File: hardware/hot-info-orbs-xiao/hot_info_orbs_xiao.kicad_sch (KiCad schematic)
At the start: 10 parts, among them SW1 SW_Push, SW2 SW_Push, SW3 SW_Push, U2 ESP32-S3-SuperMini

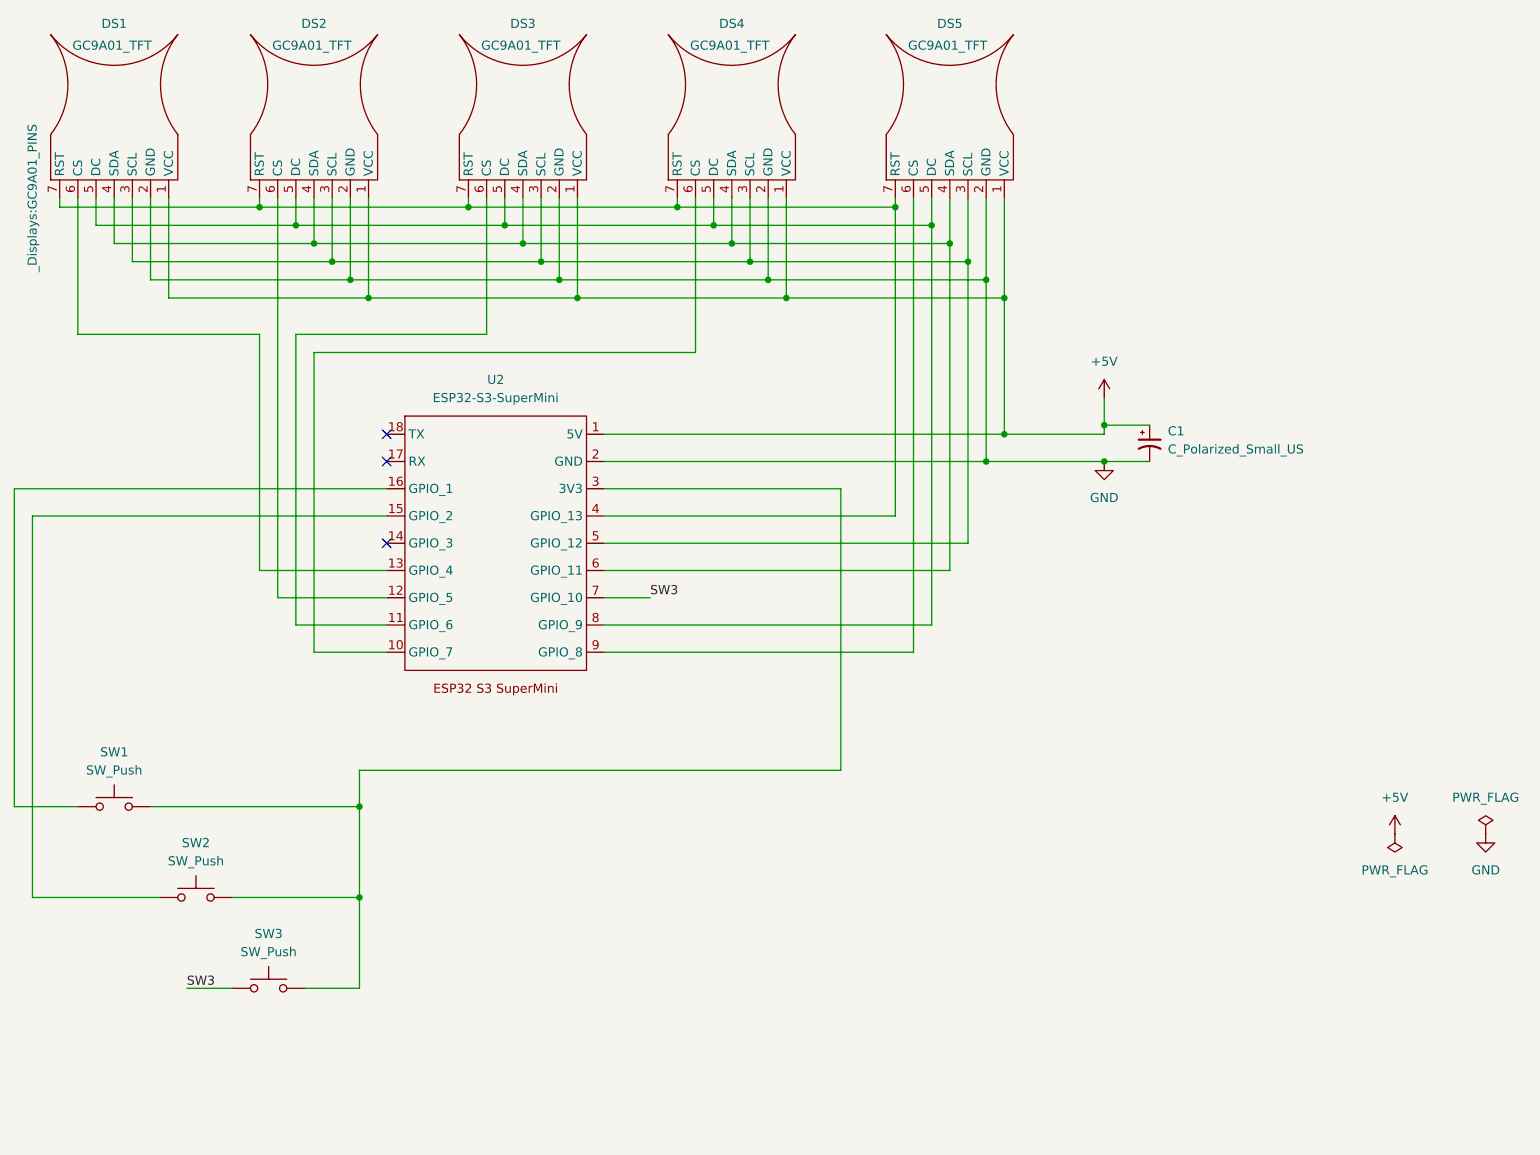
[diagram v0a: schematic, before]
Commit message: xiao: schematic + PCB swap scripts, first run (WIP checkpoint)
Schematic: SuperMini symbol out, XIAO U2 in with net labels per the pin
map, R1/C2 RC reset on /RST, ERC clean. PCB: XIAO-ESP32-S3-DIP on B.Cu,
R1/C2 on F.Cu, every pad re-netted, tracks ripped. Scripts already carry
the DRC fixes (FPID, Description, 14-pin symbol, U2 y 95, silk) but the
.kicad_sch/.kicad_pcb here are from the run BEFORE those fixes — next
commit reruns both from e6ea813. Committed mid-stream on purpose so a
model switch loses nothing.

Co-Authored-By: Claude Fable 5.1 <noreply@anthropic.com>
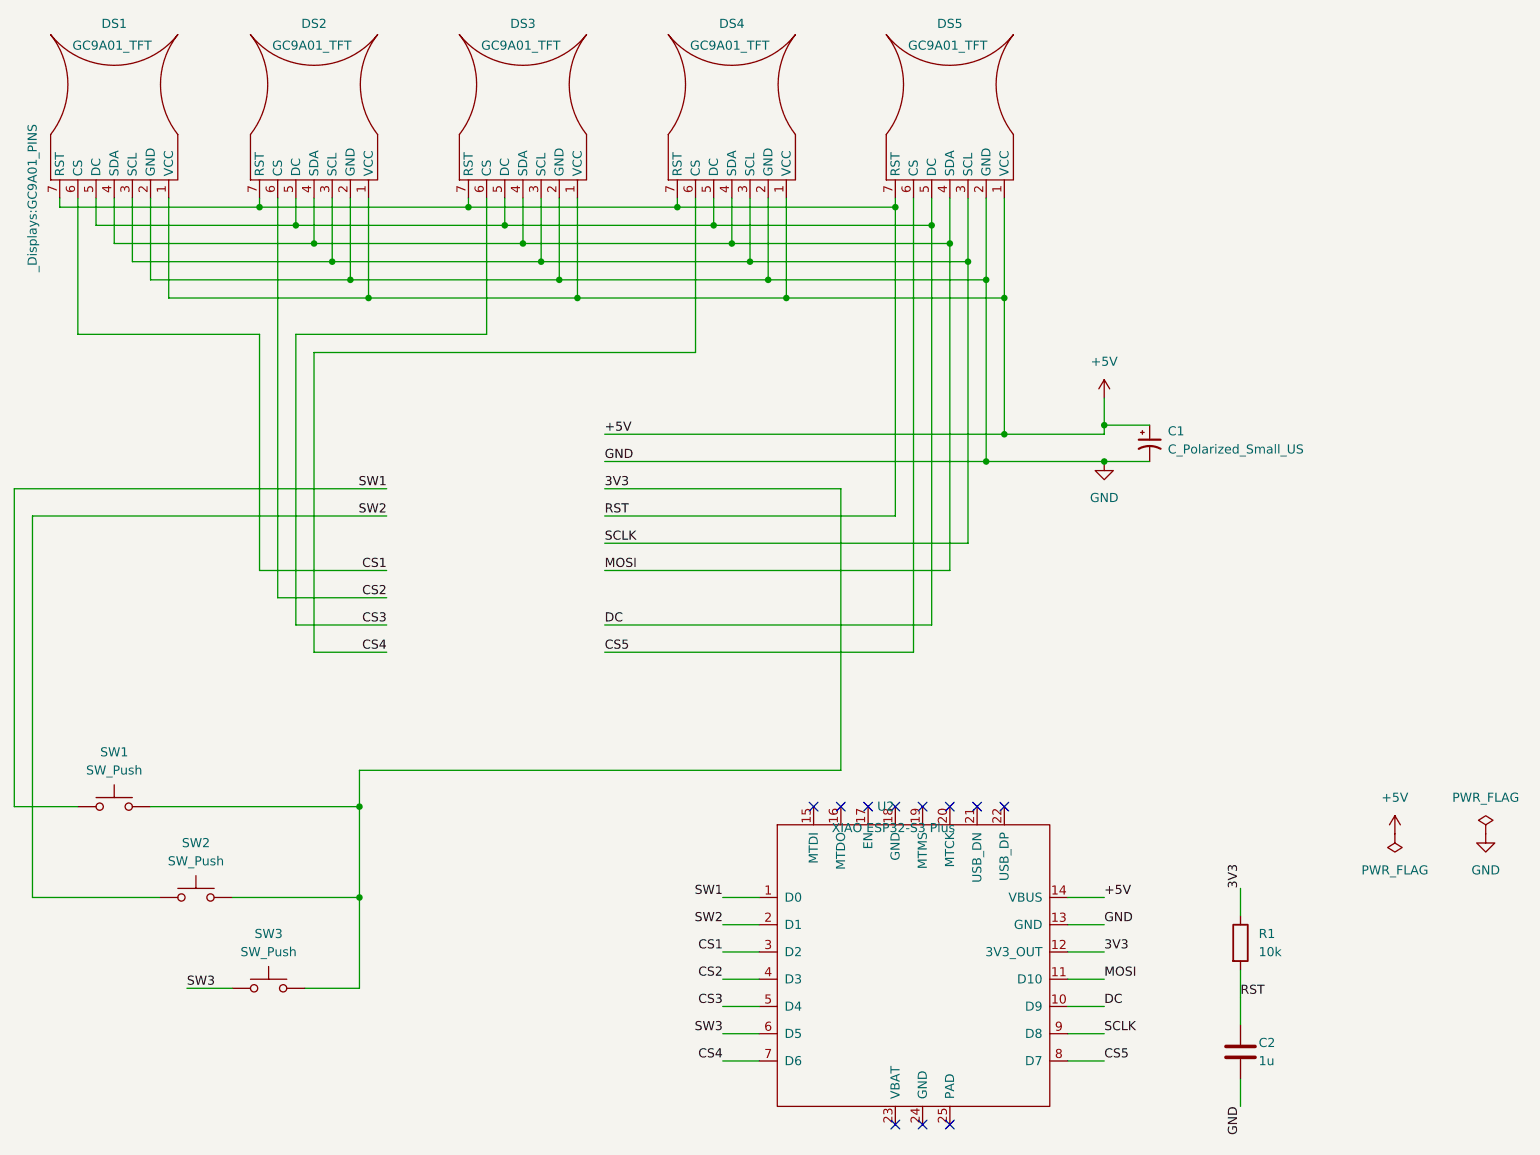
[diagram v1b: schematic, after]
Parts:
- removed U2: ESP32-S3-SuperMini, _ESP32 modules:ESP32S3-SuperMini, symbol _ESP32 modules:ESP32-S3-SuperMini
- added C2: 1u, Capacitor_THT:C_Disc_D5.0mm_W2.5mm_P5.00mm, symbol Device:C
- added R1: 10k, Resistor_THT:R_Axial_DIN0207_L6.3mm_D2.5mm_P10.16mm_Horizontal, symbol Device:R
- added U2: XIAO ESP32-S3 Plus, _ESP32 modules:XIAO-ESP32-S3-DIP, symbol _Seeed XIAO:XIAO-ESP32-S3-SMD
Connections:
- net +5V: now also U2.14 (VBUS)
- net GND: now also C2.2, U2.13 (GND)
- net SW3: now also U2.6 (D5)
- net SCLK: now reaches DS1.3 (SCL), DS2.3 (SCL), DS3.3 (SCL), DS4.3 (SCL), DS5.3 (SCL)
- net SCLK: now also U2.9 (D8)
- net MOSI: now reaches DS1.4 (SDA), DS2.4 (SDA), DS3.4 (SDA), DS4.4 (SDA), DS5.4 (SDA)
- net MOSI: now also U2.11 (D10)
- net DC: now reaches DS1.5 (DC), DS2.5 (DC), DS3.5 (DC), DS4.5 (DC), DS5.5 (DC)
- net DC: now also U2.10 (D9)
- net CS5: now reaches DS5.6 (CS)
- net CS5: now also U2.8 (D7)
- net RST: now reaches DS1.7 (RST), DS2.7 (RST), DS3.7 (RST), DS4.7 (RST), DS5.7 (RST)
- net RST: now also C2.1, R1.2
- net CS3: now reaches DS3.6 (CS)
- net CS3: now also U2.5 (D4)
- net SW1: now reaches SW1.1
- net SW1: now also U2.1 (D0)
- net 3V3: now reaches SW1.2, SW2.2, SW3.2
- net 3V3: now also R1.1, U2.12 (3V3_OUT)
- net CS4: now reaches DS4.6 (CS)
- net CS4: now also U2.7 (D6)
- net CS2: now reaches DS2.6 (CS)
- net CS2: now also U2.4 (D3)
- net CS1: now reaches DS1.6 (CS)
- net CS1: now also U2.3 (D2)
- net SW2: now reaches SW2.1
- net SW2: now also U2.2 (D1)
- no-connect marks 3 -> 11
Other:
- title: (none) -> HoT Info Orbs - XIAO ESP32-S3 variant

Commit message: xiao: schematic + PCB regenerated from e6ea813, DRC/parity clean before routing
Both swap scripts rerun against the untouched copy so the result is
reproducible rather than hand-patched. Symbol trimmed to the 14 edge pins
(renamed XIAO-ESP32-S3-edge) instead of carrying 11 no_connects that
parity flagged as pad-less. U2 moved to y 95.0 so the 21 mm module stays
inside the 107.8 edge; SuperMini silk art rewritten for the XIAO; the
B.Silk keepout rectangle removed (rule area kept). Description copied
via GetField().SetText() — SetField(FIELD_T_DESCRIPTION) makes a stray
field '5' that printed on silk and produced 134 bogus warnings.

DRC: 0 errors, 0 parity, 45 unconnected (not yet routed), 14 accepted
warnings = Seeed outline over its own castellations.

Co-Authored-By: Claude Fable 5.1 <noreply@anthropic.com>
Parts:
- removed U2: XIAO ESP32-S3 Plus, _ESP32 modules:XIAO-ESP32-S3-DIP, symbol _Seeed XIAO:XIAO-ESP32-S3-SMD
- added U2: XIAO ESP32-S3 Plus, _ESP32 modules:XIAO-ESP32-S3-DIP, symbol _Seeed XIAO:XIAO-ESP32-S3-edge
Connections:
- net +5V: now also U2.14 (VBUS)
- net 3V3: now also U2.12 (3V3_OUT)
- net CS1: now also U2.3 (D2)
- net CS2: now also U2.4 (D3)
- net CS3: now also U2.5 (D4)
- net CS4: now also U2.7 (D6)
- net CS5: now also U2.8 (D7)
- net DC: now also U2.10 (D9)
- net GND: now also U2.13 (GND)
- net MOSI: now also U2.11 (D10)
- net SCLK: now also U2.9 (D8)
- net SW1: now also U2.1 (D0)
- net SW2: now also U2.2 (D1)
- net SW3: now also U2.6 (D5)
- no-connect marks 11 -> 0
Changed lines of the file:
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@@
 		)
 	)
-	(no_connect
-		(at 156.21 146.05)
-	)
-	(no_connect
-		(at 160.02 146.05)
-	)
-	(no_connect
-		(at 163.83 146.05)
-	)
-	(no_connect
-		(at 167.64 146.05)
-	)
-	(no_connect
-		(at 171.45 146.05)
-	)
-	(no_connect
-		(at 175.26 146.05)
-	)
-	(no_connect
-		(at 179.07 146.05)
-	)
-	(no_connect
-		(at 182.88 146.05)
-	)
-	(no_connect
-		(at 167.64 190.5)
-	)
-	(no_connect
-		(at 171.45 190.5)
-	)
-	(no_connect
-		(at 175.26 190.5)
-	)
 	(symbol
-		(lib_id "_Seeed XIAO:XIAO-ESP32-S3-SMD")
+		(lib_id "_Seeed XIAO:XIAO-ESP32-S3-edge")
 		(at 170.18 160.02 0)
 		(unit 1)
@@
 		(pin "14"
 		)
-		(pin "15"
-		)
-		(pin "16"
-		)
-		(pin "17"
-		)
-		(pin "18"
-		)
-		(pin "19"
-		)
-		(pin "20"
-		)
-		(pin "21"
-		)
-		(pin "22"
-		)
-		(pin "23"
-		)
-		(pin "24"
-		)
-		(pin "25"
-		)
 		(instances

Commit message: xiao: physical rework, placed not routed (sockets, top-edge switches, no antenna patch)
Scott 2026-10-16: no antenna on the board, displays as low as possible on
headers into female sockets, right-angle 6x6x8 switches on the TOP edge
equally spaced in the centre third, C1/C2/R1 to the bottom. Physicals
first, route after he checks the STEP - so all tracks are stripped and the
pour is unfilled; DRC shows 46 unconnected and 0 parity on purpose.

- ANTENNA_PATCH and its silk removed; antenna_patch.py retired.
- DS1-5 -> new _Displays:GC9A01_SOCKET (same pads, PinSocket_1x07 model,
  display lifted 8.5 mm), pad row y 106.01 = the 0.5 mm edge rule + margin.
- SW1-3 -> stock PTS645Vx39 right-angle. Rejected the other PTS645 angled
  variants: Vx39's 8.05 mm overall depth is the one nearest "6x6x8". Its
  7.0 mm tab pitch vs the listing's 6.5 mm is unverified - measure a part.
- R1 in the DS1/DS2 gap, C1+C2 in DS3/DS4. Rejected the DS2/DS3 gap: the
  XIAO is on the back there and THT leads would hit it.
- Every Remove deferred to the end: after the first b.Remove() SWIG stops
  typing every return value, not just Zones() as HANDOFF had it.

Co-Authored-By: Claude Opus 5.5 <noreply@anthropic.com>
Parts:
- DS1, DS2, DS3, DS4, DS5: footprint _Displays:GC9A01_PINS -> _Displays:GC9A01_SOCKET
- SW1, SW2, SW3: footprint Button_Switch_THT:SW_PUSH_6mm_H5mm -> Button_Switch_THT:SW_Tactile_SPST_Angled_PTS645Vx39-2LFS
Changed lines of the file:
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@@
 			)
 		)
-		(property "Footprint" "_Displays:GC9A01_PINS"
+		(property "Footprint" "_Displays:GC9A01_SOCKET"
 			(at 163.83 60.96 0)
 			(hide yes)
@@
 			)
 		)
-		(property "Footprint" "_Displays:GC9A01_PINS"
+		(property "Footprint" "_Displays:GC9A01_SOCKET"
 			(at 104.14 60.96 0)
 			(hide yes)
@@
 			)
 		)
-		(property "Footprint" "Button_Switch_THT:SW_PUSH_6mm_H5mm"
+		(property "Footprint" "Button_Switch_THT:SW_Tactile_SPST_Angled_PTS645Vx39-2LFS"
 			(at 58.42 140.97 0)
 			(hide yes)
@@
 			)
 		)
-		(property "Footprint" "_Displays:GC9A01_PINS"
+		(property "Footprint" "_Displays:GC9A01_SOCKET"
 			(at 133.35 60.96 0)
 			(hide yes)
@@
 			)
 		)
-		(property "Footprint" "_Displays:GC9A01_PINS"
+		(property "Footprint" "_Displays:GC9A01_SOCKET"
 			(at 74.93 60.96 0)
 			(hide yes)
@@
 			)
 		)
-		(property "Footprint" "Button_Switch_THT:SW_PUSH_6mm_H5mm"
+		(property "Footprint" "Button_Switch_THT:SW_Tactile_SPST_Angled_PTS645Vx39-2LFS"
 			(at 69.85 153.67 0)
 			(hide yes)
@@
 			)
 		)
-		(property "Footprint" "_Displays:GC9A01_PINS"
+		(property "Footprint" "_Displays:GC9A01_SOCKET"
 			(at 46.99 60.96 0)
 			(show_name no)
@@
 			)
 		)
-		(property "Footprint" "Button_Switch_THT:SW_PUSH_6mm_H5mm"
+		(property "Footprint" "Button_Switch_THT:SW_Tactile_SPST_Angled_PTS645Vx39-2LFS"
 			(at 80.01 166.37 0)
 			(hide yes)

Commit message: xiao: switches on the thirds, XIAO on sockets, board ID and HOT logo on the back
Scott 2026-10-16, third physical pass. The board is still placed and not
routed.

- Switches: one on the 1/3 line, one on the 2/3 line, one midway (x 117.63
  / 150.78 / 183.92). Pass 1 had centred them in three equal slots of the
  centre third, which was a misreading.
- XIAO uses the displays' arrangement: male headers into two 1x07 female
  sockets. The new XIAO-ESP32-S3-SOCKET footprint keeps Seeed's hole
  positions, which are already at the header holes; the DIP's drill offset
  moves only the copper. Drill is 1.0 mm with 1.7 mm pads, the same as the
  display sockets. The script asserts that every pad lands on the old hole.
- Board ID moved to the back, the XIAO's side. The 5 mm HOT logo becomes a
  28 mm copy built from the same polygons, scaled. A new bitmap trace was
  rejected because the vector art holds up when scaled. Font stays Comic
  Sans as on v1.1.
- Orphan "VCC"/"GND" back labels removed: they marked nothing even on
  1d4623f.

DRC: 0 parity, 46 unconnected (no tracks), 5 silk_edge warnings (socket
tab boxes).

Co-Authored-By: Claude Opus 5.5 <noreply@anthropic.com>
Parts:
- U2: footprint _ESP32 modules:XIAO-ESP32-S3-DIP -> _ESP32 modules:XIAO-ESP32-S3-SOCKET
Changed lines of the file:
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@@
 			)
 		)
-		(property "Footprint" "_ESP32 modules:XIAO-ESP32-S3-DIP"
+		(property "Footprint" "_ESP32 modules:XIAO-ESP32-S3-SOCKET"
 			(at 170.18 160.02 0)
 			(hide yes)

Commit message: bom(xiao): Link 1 prices and build-cost total; C1 = 100uF 16V
Prices are the Link 1 listings seen live 2026-10-17, so no +40% estimate
mark. Two totals at the bottom: one build bought in whole packs ($104.50:
5 displays from a 3-pack means two packs), and the per-board share with each
pack pro-rated ($55.58). Kept both because the pack-bought figure alone hugely
overstates a club batch, and the pro-rated one alone hides what the first
board really costs. The XIAO-socket line is 0 in build cost because it comes
out of the display sockets' 60-pack. The PCB is left out of both: a JLCPCB
quote depends on quantity and colors, and guessing it would put an estimate
inside a total that is otherwise measured.

C1 value set by Scott and written into the schematic and PCB Value fields;
kicad-cli BOM shows "100uF 16V", DRC 0/0/0 with schematic parity.

Co-Authored-By: Claude Opus 5.5 <noreply@anthropic.com>
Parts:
- C1: value C_Polarized_Small_US -> 100uF 16V
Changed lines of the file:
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@@
 			)
 		)
-		(property "Value" "C_Polarized_Small_US"
+		(property "Value" "100uF 16V"
 			(at 205.74 96.0881 0)
 			(show_name no)
